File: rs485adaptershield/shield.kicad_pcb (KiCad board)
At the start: 4 copper layers, 66 x 53.3 mm, 106 parts, among them IC1 USB2422-I_MJ, IC2 THVD1406DRLR, J2 XT60, J7 RACK OUT 2.00mm, Q3 UT6KE5, U1 INA293B3, U10 TPSM33606S5QRDNRQ1, U11 MCP9700Ax-ETT, U2 Analog_1, U3 Analog_2, U5 TPSM33606S5QRDNRQ1, U6 Digital_1, U7 Digital_2, U8 AP2171W, U9 AP2171W, U901 USBLC6-2SC6, U902 USBLC6-2SC6, Y1 SG-210STF

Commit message: need to redo vias
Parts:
- moved C32 3.01 mm to (166.3, 74.1), turned to -90 degrees
- moved C40 2.88 mm to (163.4, 74.1), turned to -90 degrees
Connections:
- U2 pad 5: +5V -> unconnected-(U2-+5V-Pad5)
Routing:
- net VBATT: track 40.4 -> 62.9 mm, vias 22 -> 39
- net GND: track 97.5 -> 112.8 mm, vias 80 -> 256
- net /VBUS_OUT_B: track 14.3 -> 18.4 mm, vias 13 -> 15
- net /VBUS_OUT_A: track 13.7 -> 17.2 mm, vias 13 -> 15
- net +3.3V: vias 9 -> 8
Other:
- board text added: "TPSM33606S5QRDNRQ1"
- board text added: "{ "ViaStitching": "0.2", "GND": { "HSpacing": "3", "VSpacing": "3", "HOffset": "0", "VOffset": "0", "Clearance": "0", "Randomize": false } }"
- board text added: "{ "ViaStitching": "0.2", "GND": { "HSpacing": "4", "VSpacing": "4", "HOffset": "0", "VOffset": "0", "Clearance": "0", "Randomize": false } }"

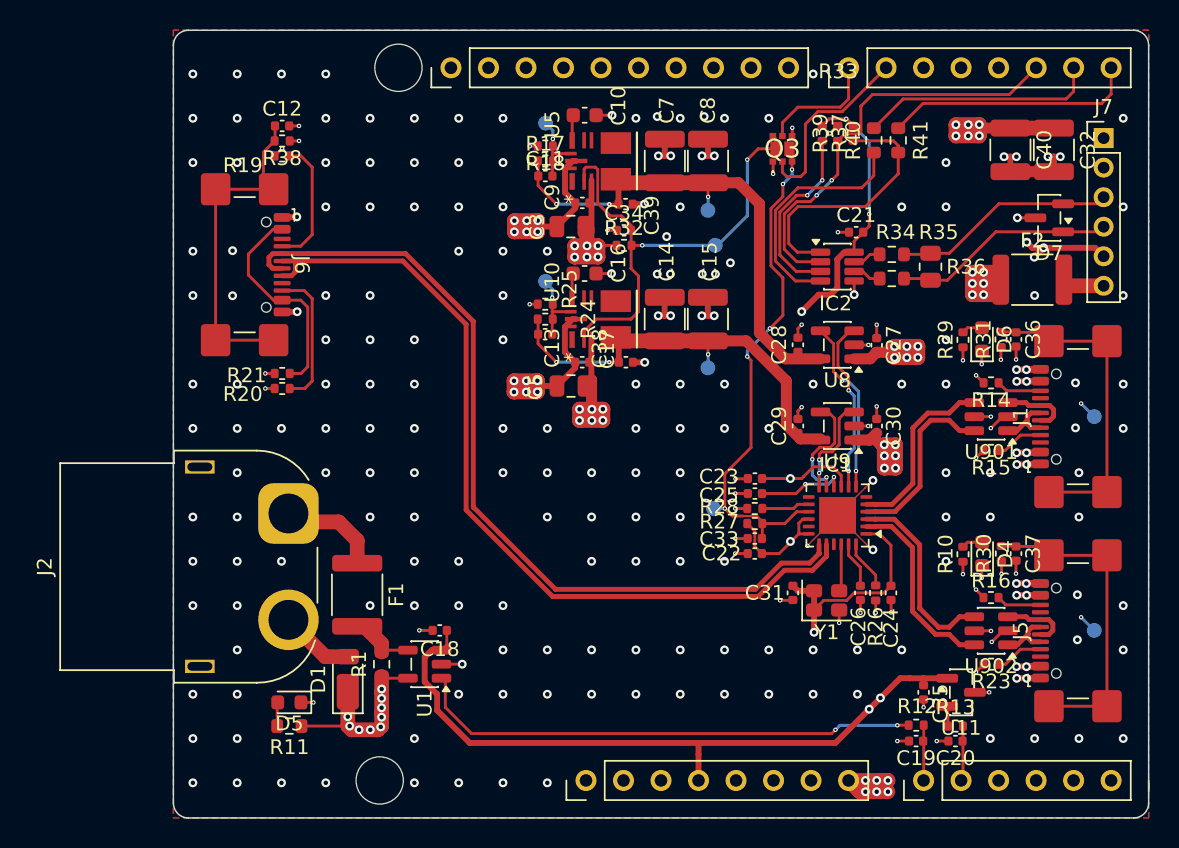
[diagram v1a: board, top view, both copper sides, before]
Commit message: fixed most via sizing issues
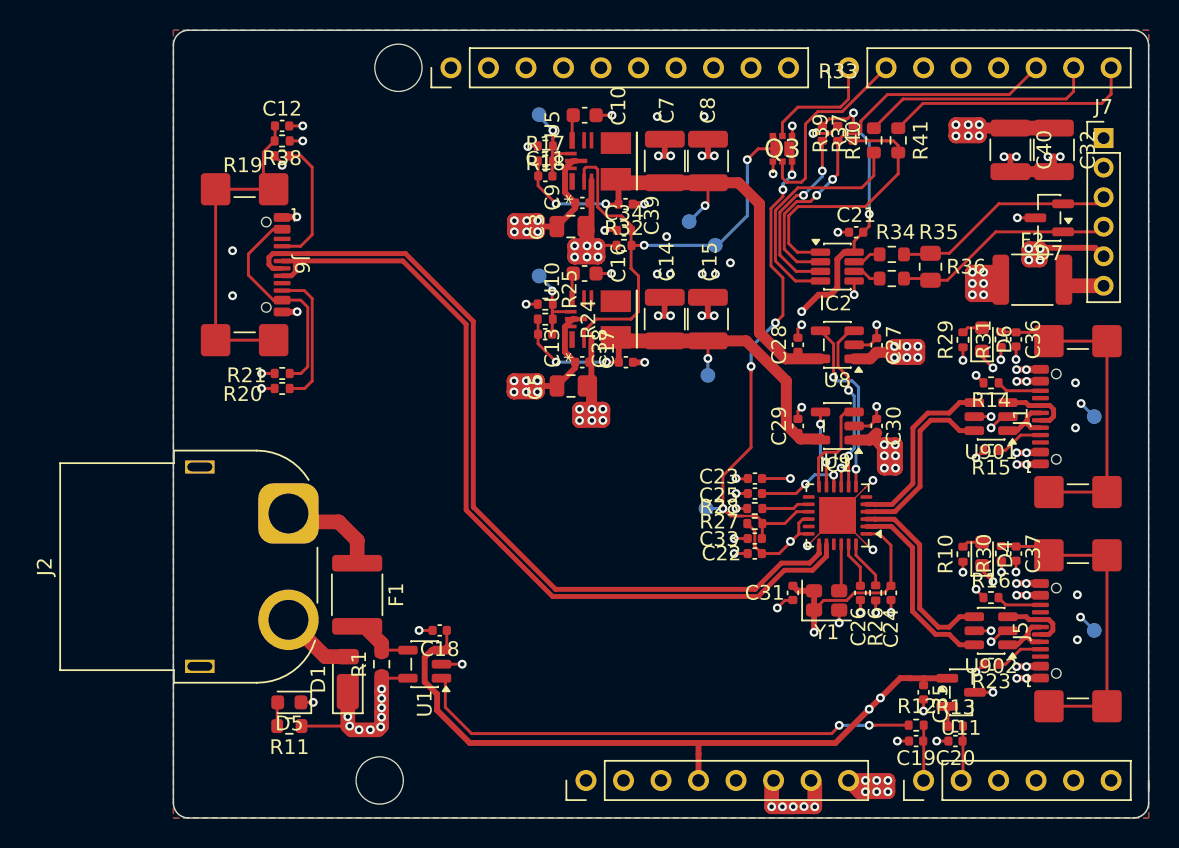
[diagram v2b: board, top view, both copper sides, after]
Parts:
- moved TP8 1.48 mm to (141.6, 79.0)
- moved TP2 0.72 mm to (131.4, 71.8)
- moved TP1 0.57 mm to (131.4, 82.7)
- moved TP5 0.51 mm to (142.7, 98.4)
- moved TP9 0.51 mm to (142.9, 89.4)
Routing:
- net GND: track 112.8 -> 127.9 mm, vias 256 -> 107
- net /USB/EN_B: track 7.87 -> 5.23 mm
- net +3.3V: track 126.1 -> 127.8 mm, vias 8 -> 9
- net VUSB_B: track 35.8 -> 37.0 mm
- net /USB_PWR_SHDN: track 12.8 -> 13.6 mm
- net VBATT: track 62.9 -> 63.7 mm
- net /Power Supply/FB1: track 5.05 -> 5.80 mm
- net /Power Supply/FB2: track 5.05 -> 5.74 mm
- net /RS485 TxRx/¬RESET: track 28.7 -> 28.1 mm
- net VUSB_A: track 29.8 -> 30.3 mm
- net /USB/¬FLG_B: track 6.79 -> 6.92 mm, vias 2 -> 0
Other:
- board text added: "{ "ViaStitching": "0.2", "GND": { "HSpacing": "2", "VSpacing": "2", "HOffset": "0", "VOffset": "0", "Clearance": "0", "Randomize": false } }"
- board text added: "{ "ViaStitching": "0.2", "GND": { "HSpacing": "2.5", "VSpacing": "2.5", "HOffset": "0", "VOffset": "0", "Clearance": "0", "Randomize": false } }"
- board text added: "{ "ViaStitching": "0.2", "GND": { "HSpacing": "4", "VSpacing": "4", "HOffset": "0", "VOffset": "0", "Clearance": "0", "Randomize": true } }"

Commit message: viaa
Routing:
- net GND: vias 107 -> 414
